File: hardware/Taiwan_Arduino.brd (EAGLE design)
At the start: 97.2 x 35.7 mm, 46 parts, among them J1 AVR_SPI_PRG_62X3_LOCK, T1 2SC, T2 2N, U1 ATMEGA328P_PDIP

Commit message: Replaace bypass cap
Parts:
- removed C6: (no value), SparkFun-Capacitors:CAP-PTH-5MM
- added C2: (no value), SparkFun-Capacitors:CPOL-RADIAL-100UF-25V
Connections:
- net +5V: now also C2.1; no longer C6.1
- net GND: now also C2.2; no longer C6.2
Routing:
- net GND: track 186.0 -> 189.3 mm
- net +5V: track 162.1 -> 162.6 mm
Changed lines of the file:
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@@
 <attribute name="VALUE" x="62.659" y="26" size="1.016" layer="21" font="vector" ratio="15" rot="R90"/>
-</element>
-<element name="C6" library="SparkFun-Capacitors" package="CAP-PTH-5MM" value="" x="78" y="21.5" smashed="yes" rot="R270">
-<attribute name="NAME" x="75.97" y="22.462" size="1.016" layer="25" font="vector" ratio="15" rot="R270"/>
-<attribute name="VALUE" x="76.476" y="22.516" size="0.4064" layer="27" rot="R270"/>
 </element>
 <element name="T1" library="transistor" package="TO92-ECB" value="2SC" x="80.7" y="15.7" smashed="yes">
@@
 <attribute name="VALUE" x="85.04" y="18.972" size="1.27" layer="27" ratio="10" rot="R180"/>
 </element>
+<element name="C2" library="SparkFun-Capacitors" package="CPOL-RADIAL-100UF-25V" value="" x="78" y="22.1" rot="R90"/>
 </elements>
 <signals>
@@
 <contactref element="FTDI" pad="6"/>
 <contactref element="U$1" pad="4"/>
-<contactref element="C6" pad="2"/>
 <wire x1="48.920403125" y1="13.33185" x2="48.920403125" y2="12.279596875" width="1.016" layer="1"/>
 <wire x1="48.920403125" y1="12.279596875" x2="49.9" y2="11.3" width="1.016" layer="1"/>
@@
 <wire x1="83.4" y1="13.4" x2="85.67" y2="15.67" width="0.8128" layer="1"/>
 <wire x1="85.67" y1="15.67" x2="85.74" y2="15.67" width="0.8128" layer="1"/>
-<wire x1="78" y1="19" x2="78.16" y2="18.84" width="0.8128" layer="16"/>
-<wire x1="78.16" y1="18.84" x2="78.16" y2="15.7" width="0.8128" layer="16"/>
+<wire x1="78.16" y1="20.67" x2="78.16" y2="15.7" width="0.8128" layer="16"/>
 <wire x1="71.423928125" y1="32.3217875" x2="73.3" y2="30.445715625" width="1.016" layer="16"/>
 <wire x1="73.3" y1="30.445715625" x2="73.3" y2="23.9" width="1.016" layer="16"/>
-<wire x1="73.3" y1="23.9" x2="78" y2="19.2" width="1.016" layer="16"/>
-<wire x1="78" y1="19.2" x2="78" y2="19" width="1.016" layer="16"/>
+<wire x1="73.3" y1="23.9" x2="77.7" y2="19.5" width="1.016" layer="16"/>
+<wire x1="77.7" y1="19.5" x2="78" y2="19.2" width="1.016" layer="16"/>
 <wire x1="21.959415625" y1="27.7282" x2="20.9" y2="26.668784375" width="0.6096" layer="16"/>
 <wire x1="20.9" y1="26.668784375" x2="20.9" y2="22.4" width="0.6096" layer="16"/>
@@
 <wire x1="12.7" y1="14.3" x2="12.7" y2="12.054" width="0.4064" layer="16"/>
 <wire x1="12.7" y1="12.054" x2="14.1" y2="10.654" width="0.4064" layer="16"/>
-<wire x1="78" y1="19" x2="77.8" y2="19" width="0.4064" layer="16"/>
-<wire x1="77.8" y1="19" x2="76.2" y2="20.6" width="0.4064" layer="16"/>
+<wire x1="77.8" y1="19" x2="77.6" y2="19.2" width="0.4064" layer="16"/>
+<wire x1="77.05" y1="19.75" x2="76.2" y2="20.6" width="0.4064" layer="16"/>
 <wire x1="76.2" y1="20.6" x2="72.5" y2="20.6" width="0.4064" layer="16"/>
 <wire x1="72.5" y1="20.6" x2="70.9" y2="19" width="0.4064" layer="16"/>
@@
 <wire x1="60.8" y1="11.7" x2="59.7" y2="11.7015" width="0.4064" layer="16"/>
 <wire x1="59.7" y1="11.7015" x2="58.031203125" y2="13.370296875" width="0.4064" layer="16"/>
+<contactref element="C2" pad="2"/>
+<contactref element="C2" pad="2"/>
+<wire x1="78" y1="20.83" x2="78" y2="19.8" width="0.8128" layer="16"/>
+<wire x1="78" y1="19.8" x2="77.7" y2="19.5" width="0.8128" layer="16"/>
+<wire x1="78.16" y1="20.67" x2="78" y2="20.83" width="0.8128" layer="16"/>
+<wire x1="78" y1="19.2" x2="77.6" y2="19.2" width="0.4064" layer="16"/>
+<wire x1="77.6" y1="19.2" x2="77.05" y2="19.75" width="0.4064" layer="16"/>
 </signal>
 <signal name="+5V">
@@
 <contactref element="U$1" pad="7"/>
 <contactref element="U$1" pad="3"/>
-<contactref element="C6" pad="1"/>
 <wire x1="19.18" y1="9.78" x2="18.4" y2="9" width="0.6096" layer="1"/>
 <wire x1="18.4" y1="9" x2="8.856615625" y2="9" width="0.6096" layer="1"/>
@@
 <wire x1="22.2" y1="25.428784375" x2="24.499415625" y2="27.7282" width="0.8128" layer="1"/>
 <contactref element="JP3" pad="1"/>
-<wire x1="78" y1="24" x2="80.19138125" y2="24" width="0.6096" layer="16"/>
 <wire x1="80.19138125" y1="24" x2="83.154171875" y2="27.062790625" width="0.6096" layer="16"/>
 <wire x1="60.6" y1="35.3" x2="54.6379625" y2="35.3" width="0.8128" layer="16"/>
@@
 <wire x1="60.6" y1="35.3" x2="63.5782125" y2="32.3217875" width="0.8128" layer="16"/>
 <wire x1="63.5782125" y1="32.3217875" x2="66.343928125" y2="32.3217875" width="0.8128" layer="16"/>
-<wire x1="78" y1="24" x2="75.87" y2="24" width="0.8128" layer="16"/>
-<wire x1="75.87" y1="24" x2="74.6" y2="25.27" width="0.8128" layer="16"/>
+<wire x1="76.5" y1="23.37" x2="74.6" y2="25.27" width="0.8128" layer="16"/>
 <wire x1="74.6" y1="25.27" x2="74.6" y2="31.7" width="0.8128" layer="16"/>
 <wire x1="74.6" y1="31.7" x2="72.4" y2="33.9" width="0.8128" layer="16"/>
@@
 <wire x1="66.343928125" y1="32.443928125" x2="66.343928125" y2="32.3217875" width="0.8128" layer="16"/>
 <wire x1="72.4" y1="33.9" x2="67.8" y2="33.9" width="0.8128" layer="16"/>
+<contactref element="C2" pad="1"/>
+<wire x1="78" y1="23.37" x2="76.5" y2="23.37" width="0.8128" layer="16"/>
+<wire x1="78" y1="23.37" x2="79.56138125" y2="23.37" width="0.8128" layer="16"/>
+<wire x1="79.56138125" y1="23.37" x2="80.19138125" y2="24" width="0.8128" layer="16"/>
 </signal>
 <signal name="N$15">

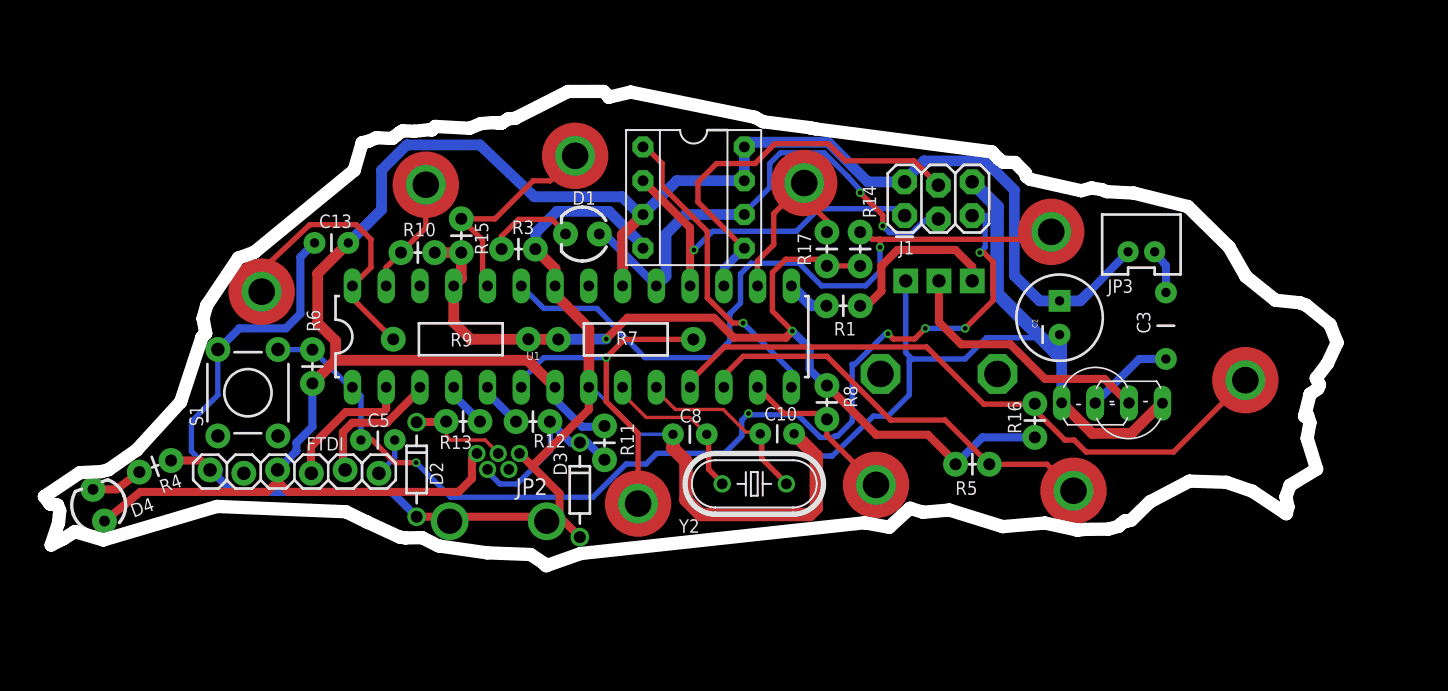
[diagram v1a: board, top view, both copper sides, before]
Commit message: Layout fixed
1.reduce via under the 328p mcu
2.fix the reset pin routing of the isp header
3.beef up the power/ground wires near C13 / reset button and USB shell
4.rotate the speaker header and transistors 45 deg
5.make more space for capacitor C1/C2
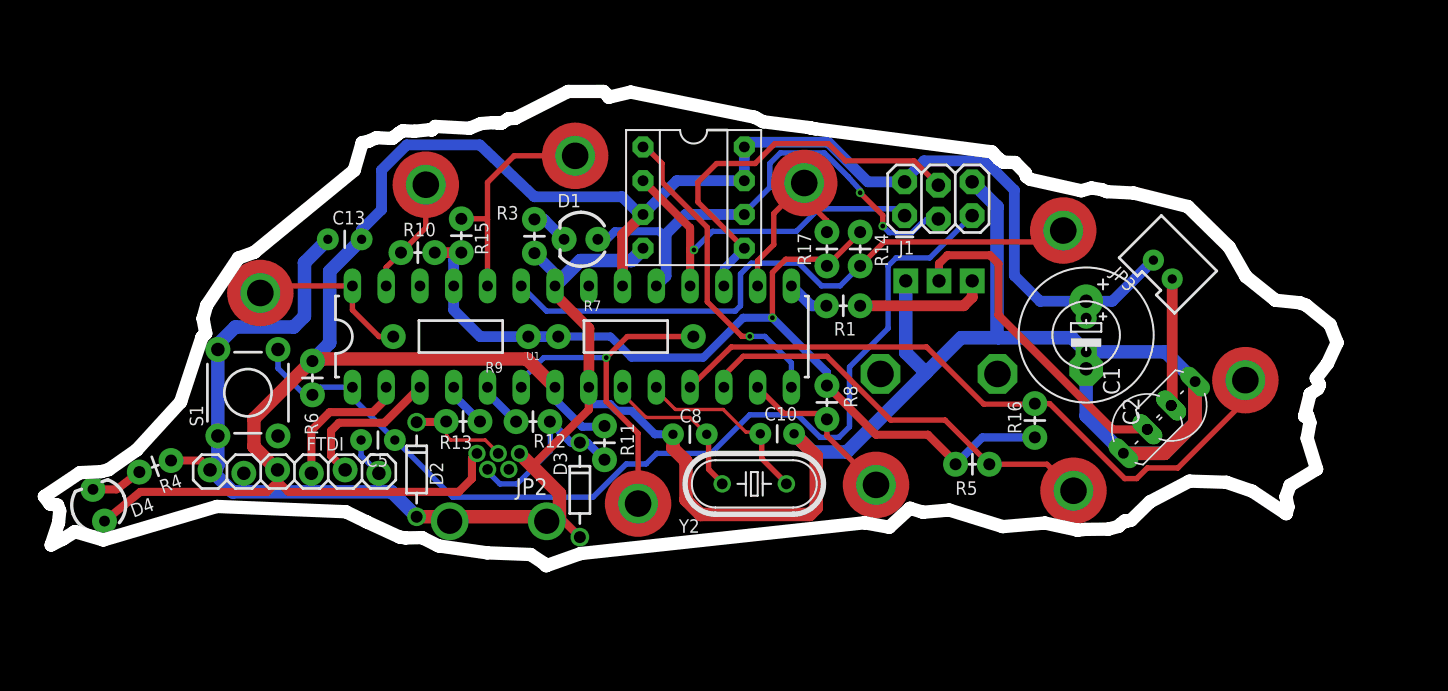
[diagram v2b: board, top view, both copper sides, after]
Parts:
- removed C3: (no value), SparkFun-Capacitors:CAP-PTH-5MM
- added C1: (no value), adafruit:E2,5-5
- C2: device SparkFun-Capacitors:CPOL-RADIAL-100UF-25V -> adafruit:E5-10,5
- moved T1 5.70 mm to (86.4, 15.5), turned to 225 degrees
- moved R6 3.40 mm to (21.8, 16.3), turned to 90 degrees
- moved R3 3.33 mm to (38.5, 29.5), turned to 270 degrees
- moved C5 2.55 mm to (28.0, 12.9), turned to 180 degrees
- moved R14 2.54 mm to (63.0, 28.5), turned to 270 degrees
- moved JP3 2.50 mm to (86.2, 26.1), turned to 315 degrees
- moved C2 2.39 mm to (80.0, 20.8), turned to 270 degrees
- moved C13 1.04 mm to (25.5, 28.0)
- moved TP9 0.91 mm to (78.3, 28.7)
- moved T2 0.54 mm to (83.7, 14.6), turned to 45 degrees
- moved D1 0.41 mm to (42.0, 28.0)
- moved R7 0.21 mm to (45.4, 20.7)
- moved R9 0.20 mm to (33.0, 20.7)
- moved TP4 0.14 mm to (17.9, 24.0)
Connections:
- removed net N$30: C3.2, JP3.2
- net +5V: now also C1.+, C2.+; no longer C2.1
- net GND: now also C1.-, C2.-; no longer C2.2
- net N$18: now also JP3.2; no longer C3.1
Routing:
- net GND: track 189.3 -> 203.3 mm
- net N$8: track 21.0 -> 12.9 mm
- net N$3: track 53.0 -> 46.9 mm, vias 1 -> 0
- net RST: track 79.8 -> 74.2 mm, vias 6 -> 0
- net +5V: track 162.6 -> 167.9 mm
- net N$22: track 19.9 -> 24.9 mm
- net N$20: track 6.80 -> 2.85 mm
- net N$30: track 3.36 -> 0.00 mm
- net N$1: track 12.9 -> 9.93 mm
- net N$18: track 6.67 -> 9.55 mm
- net N$17: track 49.1 -> 51.1 mm
- net N$14: track 10.2 -> 11.4 mm
- net N$5: track 16.4 -> 17.2 mm
- net N$11: track 71.4 -> 70.8 mm, vias 2 -> 1

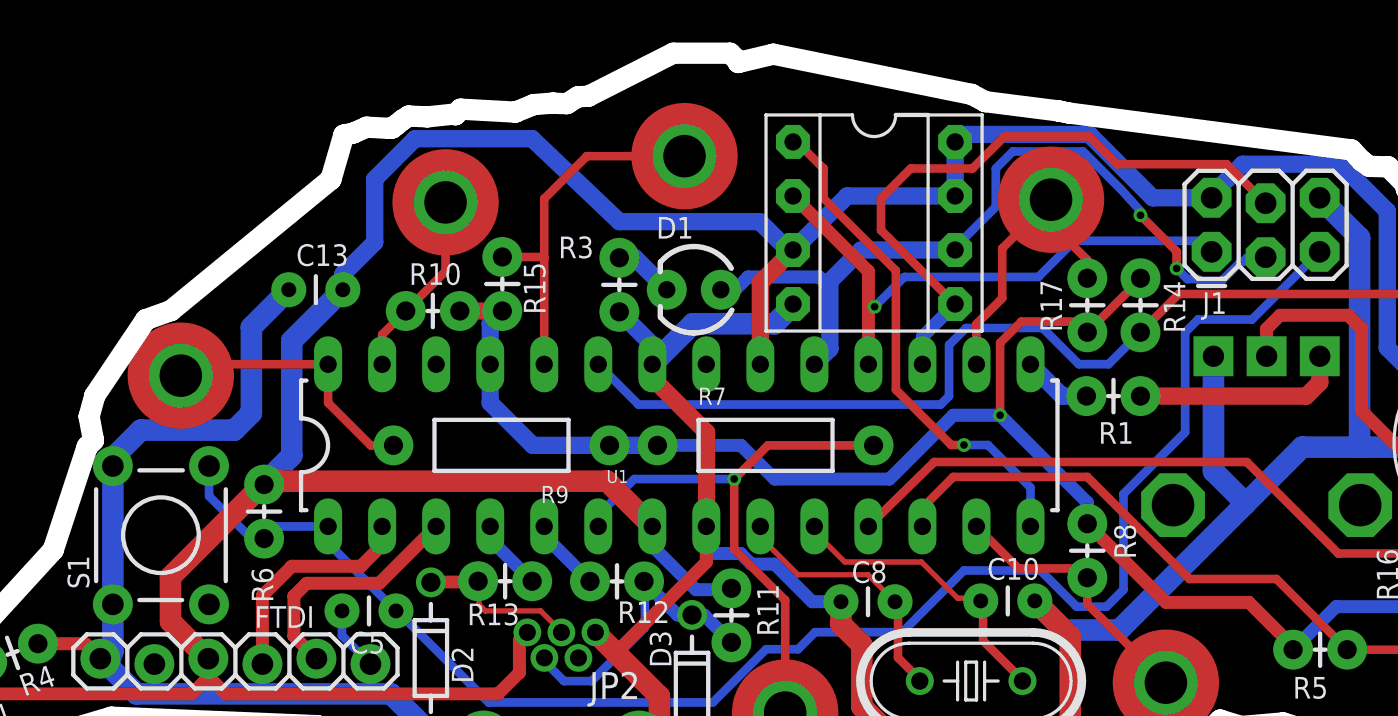
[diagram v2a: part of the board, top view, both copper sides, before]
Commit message: Added files via upload
1.change usb D+D- lines to top layer
2.reroute the VCC line between C13 and EEPROM to prevent TP1 isolated from ground plane
3.fix the SCK line from ISP header to EEPROM
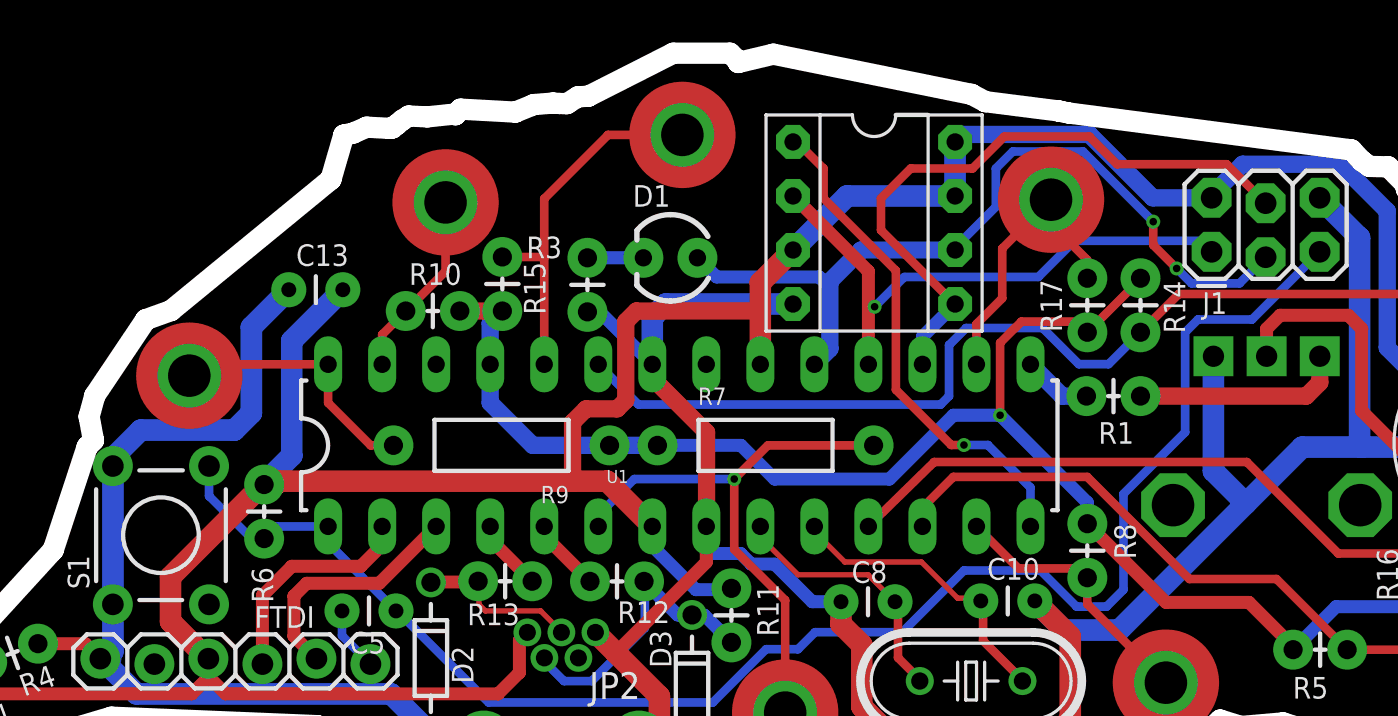
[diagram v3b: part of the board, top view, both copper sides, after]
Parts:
- moved D1 1.86 mm to (40.9, 29.5)
- moved R3 1.50 mm to (37.0, 29.5)
- moved TP1 1.00 mm to (41.5, 35.3)
- moved TP4 0.40 mm to (18.3, 24.0)
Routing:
- net +5V: track 167.9 -> 155.4 mm
- net GND: track 203.3 -> 205.5 mm
- net N$6: track 37.4 -> 38.7 mm
- net N$20: track 2.85 -> 2.23 mm

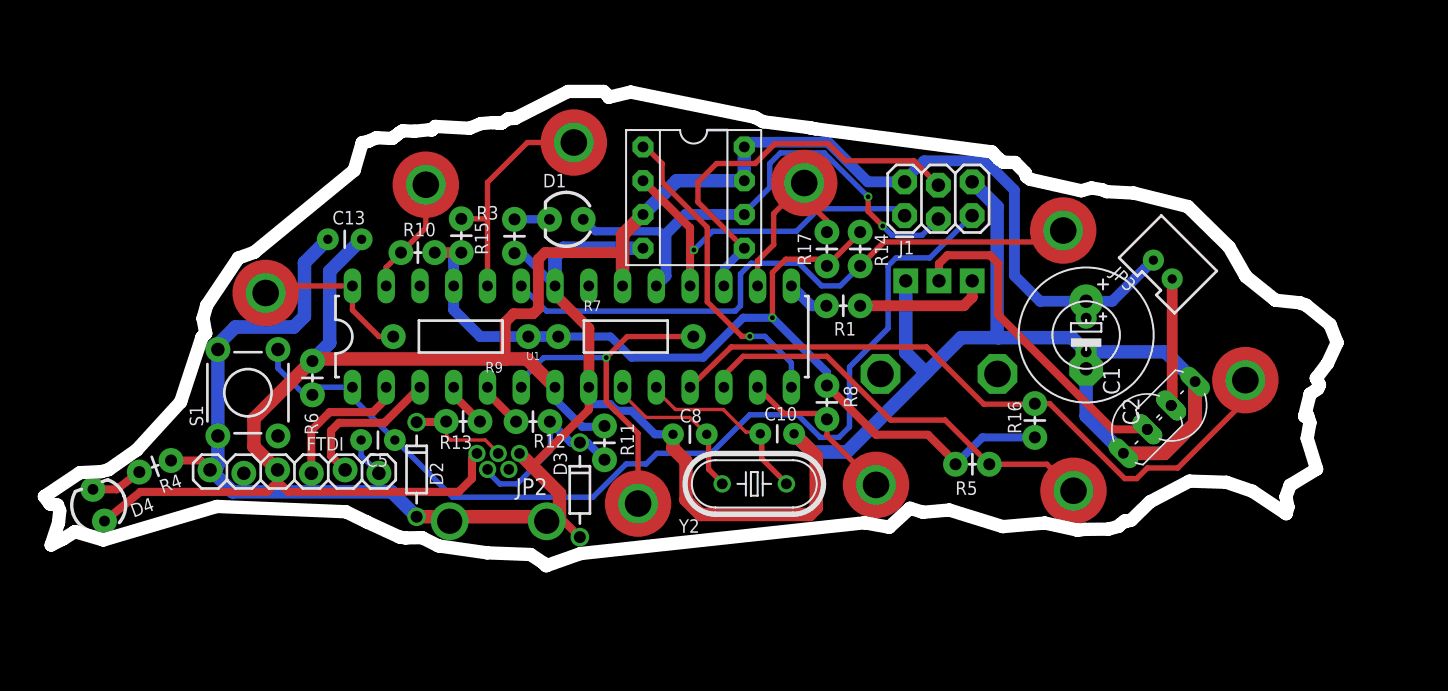
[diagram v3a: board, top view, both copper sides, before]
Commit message: Improve touch pad grounding
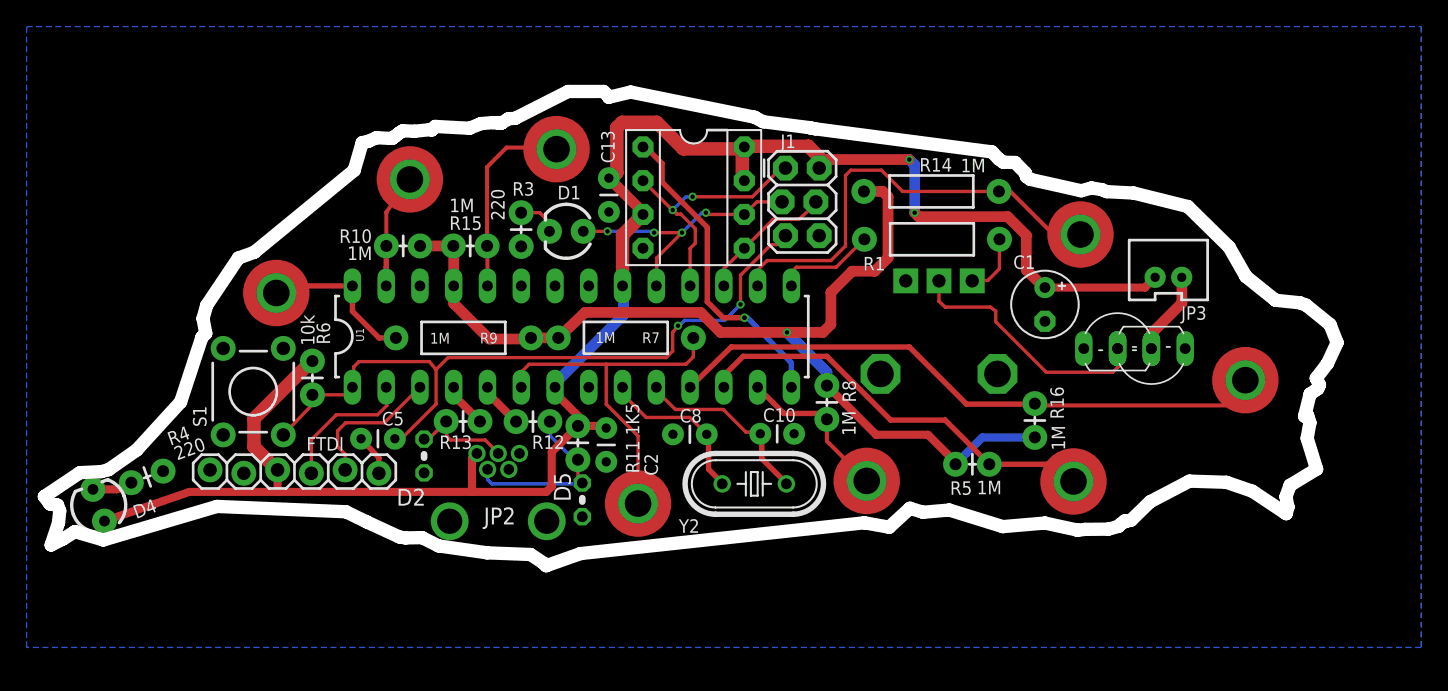
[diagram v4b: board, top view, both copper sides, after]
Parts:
- removed D3: DIODE-ZENERPTH, SparkFun-DiscreteSemi:DIODE-ZENER
- removed R17: (no value), SparkFun-Resistors:AXIAL-0.1
- removed TP7: TEST-POINT, SparkFun-Passives:PADBIG
- added D5: 3.3V, _JJG-parts:0204V
- C1: value (none) -> 100uf
- C10, C8: value (none) -> 22pf
- C13: value (none) -> 0.1uf
- C2: value (none) -> 0.1uf; device adafruit:E5-10,5 -> SparkFun-Capacitors:CAP-PTH-SMALL
- C5: value (none) -> 0.1uF
- D2: value DIODE-ZENERPTH -> 3.3V; device SparkFun-DiscreteSemi:DIODE-ZENER -> _JJG-parts:0204V
- R1: device SparkFun-Resistors:AXIAL-0.1 -> SparkFun-Resistors:AXIAL-0.4
- R10, R15, R16, R5, R7, R8, R9: value (none) -> 1M
- R11: value (none) -> 1K5
- R12, R13: value (none) -> 68
- R14: value (none) -> 1M; device SparkFun-Resistors:AXIAL-0.1 -> SparkFun-Resistors:AXIAL-0.4
- R3, R4: value (none) -> 220
- R6: value (none) -> 10k
- RV1: value (none) -> 5k
- Y2: value (none) -> 16mhz
- moved C2 36.8 mm to (43.9, 13.8)
- moved C13 19.2 mm to (44.1, 32.6), turned to 270 degrees
- moved J1 9.65 mm to (57.4, 33.4), turned to 270 degrees
- moved R1 7.36 mm to (68.4, 28.0)
- moved T2 6.59 mm to (82.4, 21.1), turned to 0 degrees
- moved R14 6.17 mm to (68.4, 31.6), turned to 0 degrees
- moved T1 4.53 mm to (84.9, 19.8), turned to 180 degrees
- moved C1 3.86 mm to (76.9, 23.1)
- moved R11 2.00 mm to (41.8, 11.4)
- moved TP1 1.39 mm to (40.2, 34.8)
- moved TP9 1.33 mm to (79.6, 28.4)
- moved TP2 1.26 mm to (29.1, 32.5)
- moved R10 1.21 mm to (29.9, 27.5)
- moved D2 1.16 mm to (30.2, 11.7), turned to 90 degrees
- moved R4 1.00 mm to (8.18, 9.69)
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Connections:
- removed net N$12: R17.P$2, TP7.P$1, U1.16
- net +5V: now also C2.1; no longer C2.+
- net GND: now also C2.2, D2.1, D5.1, S1.1; no longer C2.-, D2.P$2, D3.P$2, S1.3
- net N$11: no longer R17.P$1
- net N$15: now also D5.2; no longer D3.P$1
- net N$16: now also D2.2; no longer D2.P$1
- net N$3: now also U1.16; no longer U1.23
- net RST: now also S1.3; no longer S1.1
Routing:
- net GND: track 205.5 -> 0.00 mm
- net N$23: track 30.5 -> 10.4 mm
- net RST: track 74.2 -> 55.6 mm, vias 0 -> 2
- net N$6: track 38.7 -> 20.9 mm, vias 2 -> 4
- net +5V: track 155.4 -> 138.9 mm, vias 0 -> 2
- net N$12: track 15.2 -> 0.00 mm
- net N$3: track 46.9 -> 34.9 mm
- net N$10: track 27.1 -> 19.7 mm, vias 1 -> 2
- net N$11: track 70.8 -> 76.6 mm
- net N$22: track 24.9 -> 19.2 mm
- net N$1: track 9.93 -> 4.65 mm
- net N$2: track 3.25 -> 7.57 mm
- net N$17: track 51.1 -> 47.1 mm
- net N$18: track 9.55 -> 6.31 mm
- net N$5: track 17.5 -> 14.9 mm
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- added copper zone on layer 16, net GND
